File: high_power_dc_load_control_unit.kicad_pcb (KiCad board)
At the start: 2 copper layers, 120 x 80 mm, 83 parts, among them IC1 STPS60L45CW, IC3 LT8711EFE#TRPBF, J1 Conn_02x03_Odd_Even, J2 USB_B_Micro, J3 Conn_01x04_Socket, J4 XT60-M, J5 XT60-M, Q1 RS6P100BHTB1, Q2 PMOS, Q4 NMOS, U1 UCC5350MCD, U2 LTC3525ESC6-5-TRMPBF, U4 RT9193-33GB, U5 STM32F103C8T6, Y1 8MHz, Y2 32.768Khz

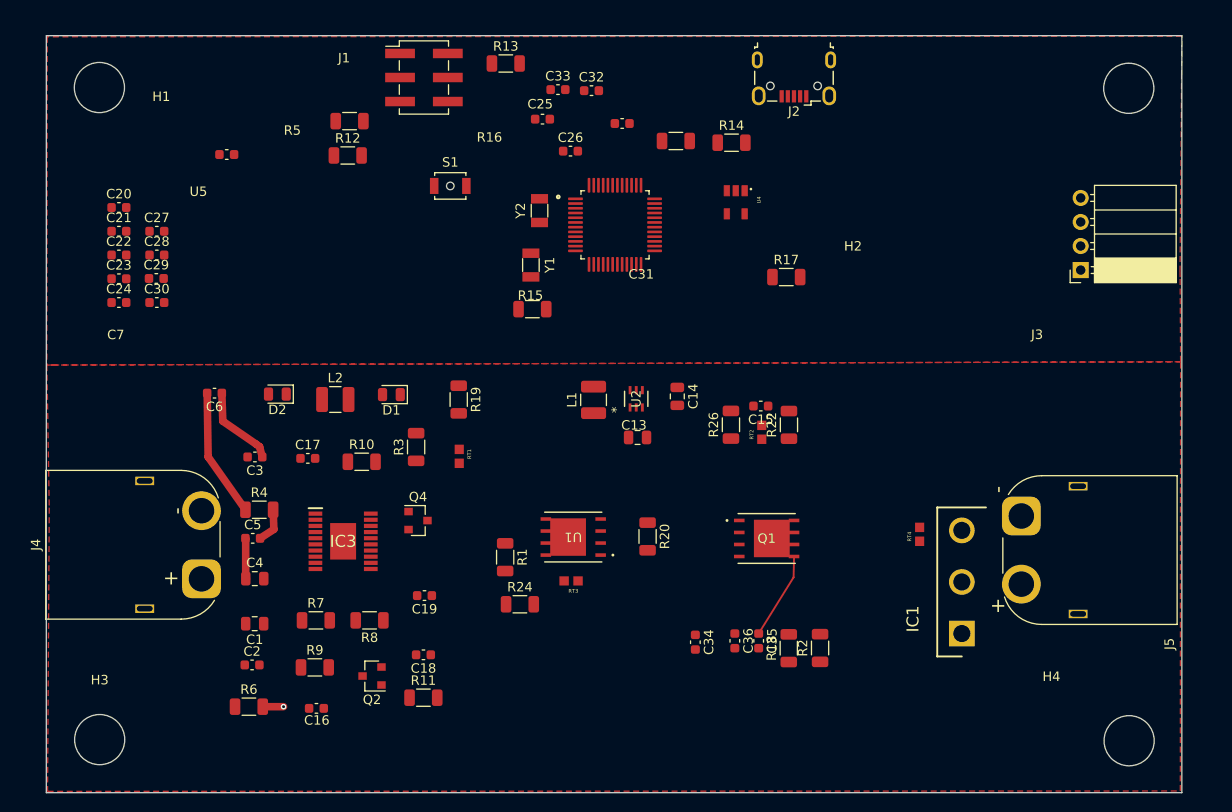
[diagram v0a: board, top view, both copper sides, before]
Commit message: Added .gitignore to prevent ZIP files from being tracked
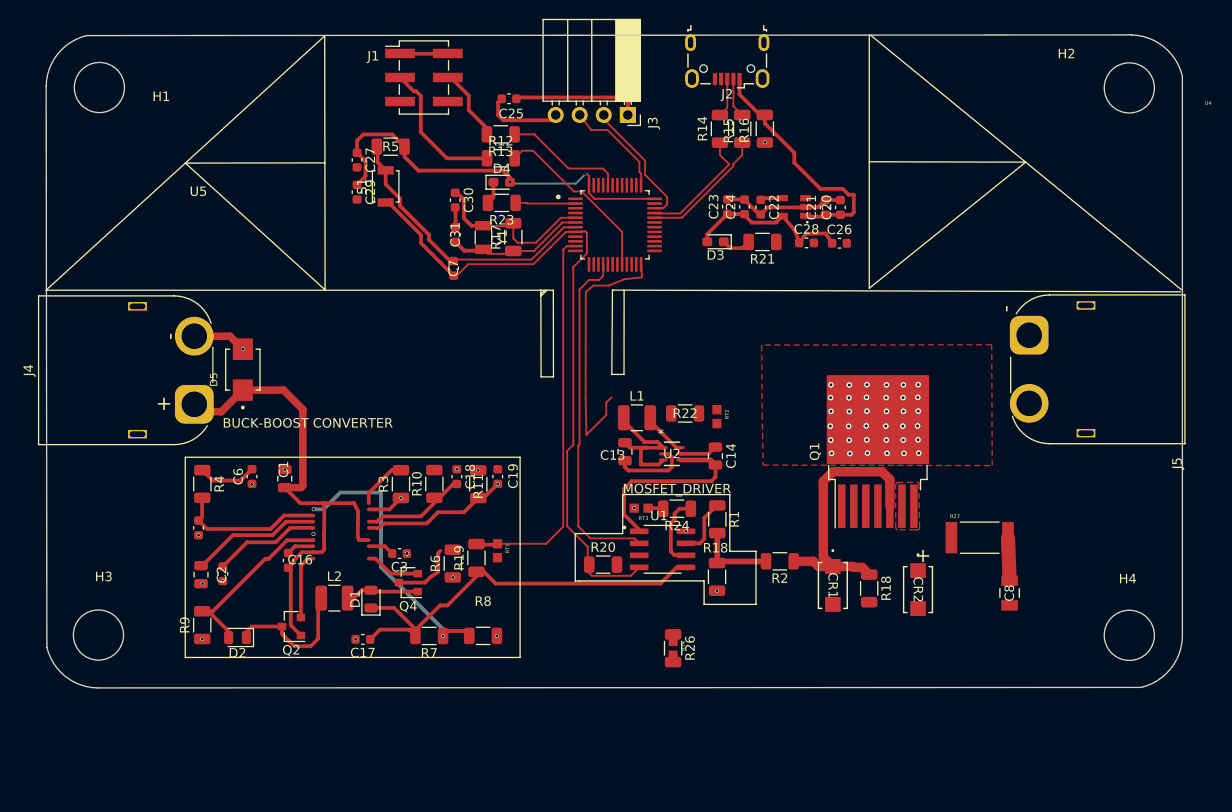
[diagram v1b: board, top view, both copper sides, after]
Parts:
- removed C15: 2.2pF, Capacitor_SMD:C_0603_1608Metric
- removed C32, C33: 20p, Capacitor_SMD:C_0603_1608Metric
- removed C34: 100nF, Capacitor_SMD:C_0603_1608Metric
- removed C35: IuF, Capacitor_SMD:C_0603_1608Metric
- removed C36: 10uF, Capacitor_SMD:C_0603_1608Metric
- removed IC1: STPS60L45CW, STPS60L45CW:TO545P515X1560X2445-3P
- removed IC3: LT8711EFE#TRPBF, AP7343-30W5-7:SOP65P640X120-21N
- removed Y2: 32.768Khz, Crystal:Crystal_SMD_3215-2Pin_3.2x1.5mm
- added C8: C1206C472K1RECAUTO, SNUBBER_CAPACITOR:CAPC340180_88N_KEM-L, F.Cu at (162.8, 105.5)
- added CR1: SMBJ13CA, SMBJ13CA:DO214AC_LTF-L, F.Cu at (144.1, 104.7)
- added CR2: SMBJ13CA, SMBJ13CA:DO214AC_LTF-L, F.Cu at (153.1, 105.1)
- added D3: LED_Small, LED_SMD:LED_0603_1608Metric_Pad1.05x0.95mm_HandSolder, F.Cu at (131.7, 68.3)
- added D4: LED_Small, LED_SMD:LED_0603_1608Metric_Pad1.05x0.95mm_HandSolder, F.Cu at (109.1, 62.0)
- added D5: SMBJ40A, SMBJ40A:DIOM4336X265N, F.Cu at (81.8, 81.9)
- added R18: 10k, Resistor_SMD:R_1206_3216Metric, F.Cu at (148.0, 105.0)
- added R21: 510, Resistor_SMD:R_1206_3216Metric, F.Cu at (136.7, 68.4)
- added R23: 510, Resistor_SMD:R_1206_3216Metric, F.Cu at (109.1, 64.2)
- added R27: 3.4, SNUBBER_RES:RESC6331X70N, F.Cu at (159.6, 99.6)
- Q1: value RS6P100BHTB1 -> IPT007N06N; footprint Library:SON8_RS6P100BHTB1_ROM-M -> Package_TO_SOT_SMD:TO-263-7_TabPin8
- R14, R15: value R -> 20
- R2: value 33 -> 4
- RT1, RT2, RT3, RT4: footprint Library:THRMC1608X95N -> NCP18XH103F03RB:THRMC1608X95N
- S1: footprint Button_Switch_SMD:SW_SPST_B3U-1000P-B -> Button_Switch_SMD:SW_SPST_B3U-1000P
- U1: footprint Library:SON8_RS6P100BHTB1_ROM-M -> UCC5350MCD:SOIC127P599X175-8N
- moved C20 76.3 mm to (144.9, 64.7), turned to 90 degrees
- moved C21 74.7 mm to (143.3, 64.7), turned to 90 degrees
- moved C28 68.7 mm to (141.3, 68.5)
- moved C22 68.0 mm to (136.5, 64.7), turned to -90 degrees
- moved C24 66.9 mm to (134.8, 64.7), turned to 90 degrees
- moved C23 64.8 mm to (133.0, 64.6), turned to 90 degrees
- moved J3 50.6 mm to (122.5, 54.9), turned to -90 degrees
- moved C30 33.3 mm to (104.2, 63.9), turned to -90 degrees
- moved C26 30.0 mm to (144.8, 68.5)
- moved R15 29.2 mm to (134.5, 56.4), turned to 90 degrees
- moved R17 29.2 mm to (110.3, 67.8), turned to 90 degrees
- moved RT4 28.7 mm to (127.2, 111.3), turned to -90 degrees
- moved C7 26.8 mm to (104.0, 71.2), turned to -90 degrees
- moved R6 26.3 mm to (104.0, 102.3), turned to 90 degrees
- moved D2 26.1 mm to (81.2, 110.2)
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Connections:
- net /FEEDBACK_LINE renamed /FB
- net /SW_PIN renamed /SW
- net Net-(D2-A) renamed /ISN
- net Net-(IC3-CSN) renamed /CSN
- net Net-(IC3-CSP) renamed /CSP
- net Net-(Q4-S) renamed /NMOS_S<->R6
- net Net-(R10-Pad2) renamed /R10_2
- net Net-(R11-Pad2) renamed /R11_2
- net Net-(U1-CLAMP) renamed /CLAMP
- net Net-(U1-IN-) renamed /IN-
- C1 pad 1: /Vin -> VIN_DC-DC_CONV
- C1 pad 2: MOSFET_DRAIN_OUT -> GNDD
- C13 pad 2: /VCC3V3 -> /*SHDN
- C16 pad 1: Net-(IC3-INTVEE) -> /INTVEE
- C16 pad 2: /Vin -> VIN_DC-DC_CONV
- C17 pad 2: Net-(C17-Pad2) -> GNDD
- C18 pad 1: MOSFET_DRAIN_OUT -> GNDD
- C19 pad 1: MOSFET_DRAIN_OUT -> GNDD
- C2 pad 1: MOSFET_DRAIN_OUT -> GNDD
- C20 pad 1: /MCU/5V -> GNDD
- C20 pad 2: MOSFET_DRAIN_OUT -> GNDD
- C21 pad 1: /MCU/5V -> GNDD
- C21 pad 2: MOSFET_DRAIN_OUT -> GNDD
- C22 pad 1: unconnected-(C22-Pad1) -> /MCU/BP
- C22 pad 2: MOSFET_DRAIN_OUT -> GNDD
- C23 pad 2: MOSFET_DRAIN_OUT -> GNDD
- C24 pad 2: MOSFET_DRAIN_OUT -> GNDD
- C25 pad 1: Net-(J3-Pin_1) -> VCC3V3
- C25 pad 2: MOSFET_DRAIN_OUT -> GNDD
- C26 pad 2: MOSFET_DRAIN_OUT -> GNDD
- C27 pad 2: MOSFET_DRAIN_OUT -> GNDD
- C28 pad 2: MOSFET_DRAIN_OUT -> GNDD
- C29 pad 2: MOSFET_DRAIN_OUT -> GNDD
- C3 pad 1: MOSFET_DRAIN_OUT -> GNDD
- C3 pad 2: Net-(IC3-INTVCC) -> /INTVCC
- C4 pad 1: MOSFET_DRAIN_OUT -> GNDD
- C4 pad 2: Net-(IC3-SS) -> /SS
- C5 pad 1: MOSFET_DRAIN_OUT -> GNDD
- C6 pad 1: MOSFET_DRAIN_OUT -> GNDD
- C7 pad 2: MOSFET_DRAIN_OUT -> GNDD
- J1 pad 5: MOSFET_DRAIN_OUT -> GNDD
- J1 pad 6: MOSFET_DRAIN_OUT -> GNDD
- J2 pad 1: /MCU/5V -> GNDD
- J2 pad 2: Net-(J2-D-) -> /MCU/D-
- J2 pad 3: Net-(J2-D+) -> /MCU/D+
- J2 pad 4: MOSFET_DRAIN_OUT -> GNDD
- J2 pad 5: MOSFET_DRAIN_OUT -> GNDD
- J2 pad 6: MOSFET_DRAIN_OUT -> GNDD
- J3 pad 1: Net-(J3-Pin_1) -> VCC3V3
- J3 pad 4: MOSFET_DRAIN_OUT -> GNDD
- L1 pad 1: /VCC3V3 -> VCC3V3
- Q1 pad 1: /mos_gate_input -> /Q1_1
- Q1 pad 2: MOSFET_DRAIN_OUT -> VIN_DC-DC_CONV
- Q1 pad 3: MOSFET_DRAIN_OUT -> GNDD
- Q1 pad 4: MOSFET_DRAIN_OUT -> (no net)
- Q1 pad 5: NTC_2_IN -> (no net)
- Q1 pad 6: NTC_2_IN -> (no net)
- Q1 pad 7: NTC_2_IN -> (no net)
- Q1 pad 8: NTC_2_IN -> (no net)
- Q2 pad 1: /Vin -> VIN_DC-DC_CONV
- Q2 pad 2: Net-(IC3-TG) -> /TG
- Q4 pad 2: Net-(IC3-BG) -> /BG
- R1 pad 2: NTC_3_IN -> MOS_DRIVE_TRIGGER
- R12 pad 2: /MCU/BOOT0 -> /MCU/BOOT1
- R13 pad 1: /MCU/BOOT1 -> /MCU/BOOT0
- R14 pad 2: Net-(J2-D+) -> /MCU/D+
- R15 pad 2: Net-(J2-D-) -> /MCU/D-
- R16 pad 2: /MCU/5V -> GNDD
- R18 pad 2: MOSFET_DRAIN_OUT -> GNDD
- R19 pad 2: NTC_1 -> NTC_1_OUT
- R2 pad 1: MOS_DRIVE_TRIGGER -> /Q1_1
- R2 pad 2: /mos_gate_input -> MOS_DRIVE_TRIGGER
- R20 pad 1: /MCU/PWM_SIGNAL -> GNDD
- R22 pad 1: NTC_2_IN -> GNDD
- R24 pad 1: NTC_3_IN -> MOS_DRIVE_TRIGGER
- R26 pad 1: MOSFET_DRAIN_OUT -> NTC_4_IN
- R3 pad 1: MOSFET_DRAIN_OUT -> GNDD
- R3 pad 2: Net-(IC3-RT) -> /RT
- R6 pad 1: MOSFET_DRAIN_OUT -> GNDD
- R8 pad 2: Net-(C17-Pad2) -> GNDD
- R9 pad 1: MOSFET_DRAIN_OUT -> GNDD
- RT1 pad 1: NTC_1 -> NTC_1_OUT
- RT1 pad 2: MOSFET_DRAIN_OUT -> GNDD
- RT2 pad 2: MOSFET_DRAIN_OUT -> GNDD
- RT3 pad 2: MOSFET_DRAIN_OUT -> GNDD
- RT4 pad 2: MOSFET_DRAIN_OUT -> GNDD
- S1 pad 1: MOSFET_DRAIN_OUT -> GNDD
- U1 pad 1: unconnected-(U1-VCC1-Pad1) -> /5V
- U1 pad 2: unconnected-(U1-IN+-Pad2) -> PWM_SIGNAL
- U1 pad 4: /GND_A -> GNDD
- U1 pad 5: Vout_12V -> /EXTVCC
- U1 pad 6: unconnected-(U1-OUT-Pad6) -> MOS_DRIVE_TRIGGER
- U1 pad 8: unconnected-(U1-VEE2-Pad8) -> GNDD
- U2 pad 1: /VCC3V3 -> /*SHDN
- U2 pad 3: /VCC3V3 -> /*SHDN
- U2 pad 5: MOSFET_DRAIN_OUT -> GNDD
- U4 pad 1: unconnected-(U4-VIN-Pad1) -> /MCU/5V
- U4 pad 2: unconnected-(U4-GND-Pad2) -> GNDD
- U4 pad 3: unconnected-(U4-EN-Pad3) -> /MCU/5V
- U4 pad 4: unconnected-(U4-BP-Pad4) -> /MCU/BP
- U4 pad 5: unconnected-(U4-VOUT-Pad5) -> VCC3V3
- U5 pad 11: unconnected-(U5-PA1-Pad11) -> NTC_1_OUT
- U5 pad 12: unconnected-(U5-PA2-Pad12) -> NTC_2_OUT
- U5 pad 13: unconnected-(U5-PA3-Pad13) -> NTC_3_OUT
- U5 pad 14: unconnected-(U5-PA4-Pad14) -> NTC_4_OUT
- U5 pad 16: unconnected-(U5-PA6-Pad16) -> PWM_SIGNAL
- U5 pad 2: unconnected-(U5-PC13-TAMPER-RTC-Pad2) -> /MCU/PC13-LED_IN
- U5 pad 20: unconnected-(U5-PB2-Pad20) -> /MCU/BOOT1
- U5 pad 23: Net-(U5-VSS-Pad23) -> GNDD
- U5 pad 24: Net-(U5-VDD-Pad24) -> VCC3V3
- U5 pad 32: unconnected-(U5-PA11-Pad32) -> /MCU/D-
- U5 pad 33: unconnected-(U5-PA12-Pad33) -> /MCU/D+
- U5 pad 34: unconnected-(U5-PA13-Pad34) -> /MCU/SWDIO
- U5 pad 35: Net-(U5-VSS-Pad23) -> GNDD
- U5 pad 36: Net-(U5-VDD-Pad24) -> VCC3V3
- U5 pad 37: unconnected-(U5-PA14-Pad37) -> /MCU/SWDCLK
- U5 pad 44: unconnected-(U5-BOOT0-Pad44) -> /MCU/BOOT0
- U5 pad 47: Net-(U5-VSS-Pad23) -> GNDD
- U5 pad 48: Net-(U5-VDD-Pad24) -> VCC3V3
- U5 pad 5: unconnected-(U5-PD0_OSC_IN-Pad5) -> /MCU/OSCIN
- U5 pad 6: unconnected-(U5-PD1_OSC_OUT-Pad6) -> /MCU/OSCOUT
- U5 pad 7: unconnected-(U5-NRST-Pad7) -> /MCU/RESET
- U5 pad 8: unconnected-(U5-VSSA-Pad8) -> GNDD
- U5 pad 9: unconnected-(U5-VDDA-Pad9) -> VCC3V3
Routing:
- net GNDD: track 0.00 -> 108.7 mm, vias 0 -> 17
- net VCC3V3: track 0.00 -> 107.4 mm, vias 0 -> 2
- net VIN_DC-DC_CONV: track 0.00 -> 54.0 mm
- net Vout_12V: track 0.00 -> 45.3 mm
- net NTC_1_OUT: track 0.00 -> 40.9 mm
- net PWM_SIGNAL: track 0.00 -> 36.6 mm
- net /MCU/RESET: track 0.00 -> 30.0 mm
- net /FB: track 0.00 -> 29.0 mm, vias 0 -> 2
- net /Q1_1: track 0.00 -> 28.7 mm
- net /MCU/5V: track 0.00 -> 27.1 mm
- net /5V: track 0.00 -> 20.5 mm
- net /ISN: track 0.00 -> 19.2 mm
- net /MCU/BOOT1: track 0.00 -> 18.7 mm
- net /MCU/OSCIN: track 0.00 -> 18.3 mm
- net /MCU/D-: track 0.00 -> 17.6 mm
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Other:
- board size 120 x 80 mm -> 120.1 x 69 mm
- board text added: "BUCK-BOOST CONVERTER"
- board text added: "MOSFET_DRIVER"

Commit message: Fix remote issue
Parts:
- added IC3: LT8711EFE#TRPBF, AP7343-30W5-7:SOP65P640X120-21N, F.Cu at (92.1, 98.9)
- moved R26 37.2 mm to (163.4, 102.9)
- moved RT4 37.1 mm to (164.1, 106.9), turned to 0 degrees
- moved S1 5.56 mm to (99.5, 67.4)
- moved R5 5.40 mm to (100.5, 62.7)
- moved C29 5.24 mm to (96.4, 58.5), turned to 90 degrees
- moved R27 3.66 mm to (157.5, 102.6)
- moved C8 3.59 mm to (159.4, 106.7), turned to 180 degrees
- moved C27 3.39 mm to (96.4, 61.9)
- moved CR2 2.62 mm to (150.6, 104.3)
- moved R20 2.26 mm to (117.8, 101.6)
- moved L1 1.89 mm to (122.0, 85.7)
- moved C13 1.78 mm to (120.7, 89.5)
- moved R18 1.74 mm to (132.5, 102.1)
- moved R18 1.46 mm to (146.6, 104.5), turned to 90 degrees
- moved R22 1.36 mm to (128.0, 85.2)
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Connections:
- C1 pad 2: GNDD -> DC-DC_CONV_GND
- C17 pad 2: GNDD -> DC-DC_CONV_GND
- C18 pad 1: GNDD -> DC-DC_CONV_GND
- C19 pad 1: GNDD -> DC-DC_CONV_GND
- C2 pad 1: GNDD -> DC-DC_CONV_GND
- C3 pad 1: GNDD -> DC-DC_CONV_GND
- C4 pad 1: GNDD -> DC-DC_CONV_GND
- C5 pad 1: GNDD -> DC-DC_CONV_GND
- C6 pad 1: GNDD -> DC-DC_CONV_GND
- J5 pad 2: (no net) -> GNDD
- L1 pad 1: VCC3V3 -> /*SHDN
- R3 pad 1: GNDD -> DC-DC_CONV_GND
- R6 pad 1: GNDD -> DC-DC_CONV_GND
- R8 pad 2: GNDD -> DC-DC_CONV_GND
- R9 pad 1: GNDD -> DC-DC_CONV_GND
- RT1 pad 2: GNDD -> DC-DC_CONV_GND
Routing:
- net DC-DC_CONV_GND: track 5.71 -> 145.3 mm, vias 1 -> 17
- net NTC_4_OUT: track 0.00 -> 94.3 mm, vias 0 -> 2
- net GNDD: track 108.7 -> 166.2 mm, vias 17 -> 7
- net MOS_OUT: track 4.40 -> 48.5 mm
- net VCC3V3: track 107.4 -> 123.5 mm, vias 2 -> 3
- net /Q1_1: track 28.7 -> 14.1 mm
- net VIN_DC-DC_CONV: track 54.0 -> 67.5 mm
- net /*SHDN: track 14.8 -> 6.70 mm
- net /MCU/RESET: track 30.0 -> 24.3 mm
- net /SW: track 4.74 -> 6.76 mm
- net MOS_DRIVE_TRIGGER: track 16.3 -> 15.2 mm
- net /CLAMP: track 6.27 -> 7.13 mm
- net /5V: track 20.5 -> 21.3 mm
- net /CSN: vias 1 -> 0
- net /R11_2: vias 1 -> 0
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- added copper zone on B.Cu, net /IN-
- added copper zone on B.Cu, net GNDD
